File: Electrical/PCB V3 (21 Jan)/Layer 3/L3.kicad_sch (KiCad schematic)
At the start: 21 parts, among them J1 Conn_01x06, J2 Conn_02x04_Counter_Clockwise, J3 Conn_01x06, J4 Conn_01x06, J5 Conn_01x06, U2 113991054, U3 4754

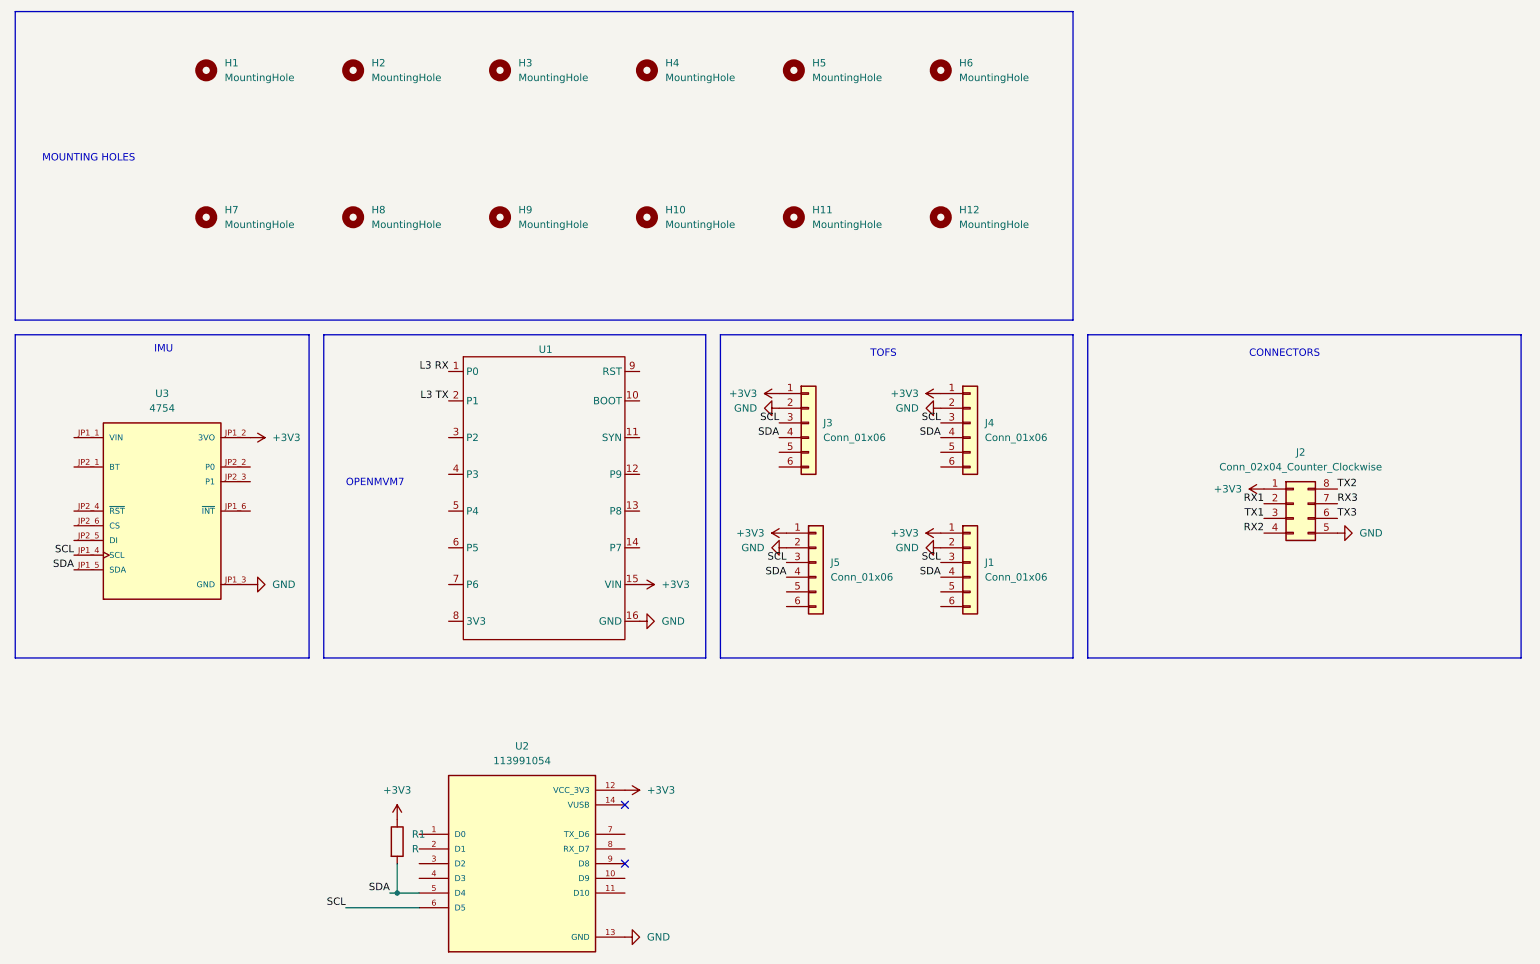
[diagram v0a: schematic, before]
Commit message: edited l3 schematics
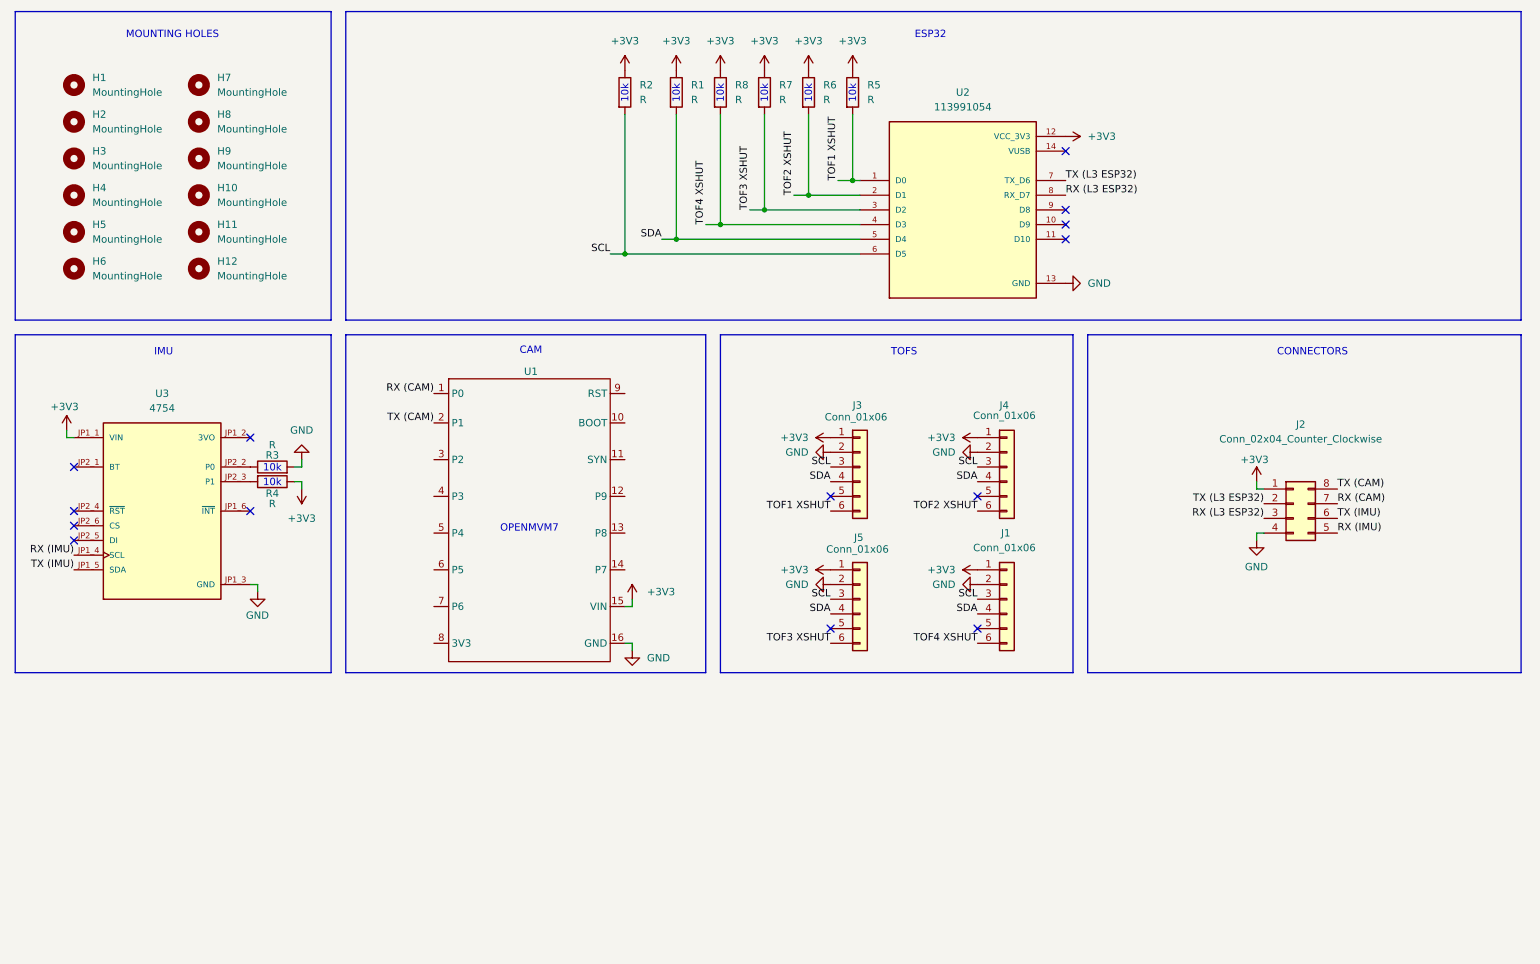
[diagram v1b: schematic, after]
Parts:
- added R2, R3, R4, R5, R6, R7, R8: R, symbol Device:R
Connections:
- net RX1 is gone; now on net TX (L3 ESP32): J2.2 (Pin_2)
- net RX2 is gone; now on net GND: J2.4 (Pin_4)
- net RX3 is gone; now on net RX (CAM): J2.7 (Pin_7)
- net TX1 is gone; now on net RX (L3 ESP32): J2.3 (Pin_3)
- net TX2 is gone; now on net TX (CAM): J2.8 (Pin_8)
- net +3V3: now also U3.JP1_1 (VIN), R2.1, R4.1, R5.1, R6.1, R7.1, R8.1; no longer U3.JP1_2 (3VO)
- net GND: now also R3.2; no longer J2.5 (Pin_5)
- net SCL: now also R2.2; no longer U3.JP1_4 (SCL)
- net SDA: no longer U3.JP1_5 (SDA)
- net TOF2 XSHUT: now reaches J4.6 (Pin_6)
- net TOF2 XSHUT: now also U2.2 (D1), R6.2
- net TOF4 XSHUT: now reaches J1.6 (Pin_6)
- net TOF4 XSHUT: now also U2.4 (D3), R8.2
- net TOF1 XSHUT: now reaches J3.6 (Pin_6)
- net TOF1 XSHUT: now also U2.1 (D0), R5.2
- net at U3.JP2_2 (P0): now also R3.1
- net at U3.JP2_3 (P1): now also R4.2
- net TOF3 XSHUT: now reaches U2.3 (D2)
- net TOF3 XSHUT: now also J5.6 (Pin_6), R7.2
- net TX (L3 ESP32): now reaches U2.7 (TX_D6)
- net RX (L3 ESP32): now reaches U2.8 (RX_D7)
- net L3 RX renamed RX (CAM)
- net L3 TX renamed TX (CAM)
- net TX3 renamed TX (IMU)
- net TX (IMU): now also U3.JP1_5 (SDA)
- new net RX (IMU): J2.5 (Pin_5), U3.JP1_4 (SCL)
- no-connect marks 2 -> 14
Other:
- note added: "10k"
- note added: "CAM"
- note added: "ESP32"
- moved on the sheet: H1, H10, H11, H12, H2, H3, H4, H5, H6, H7, H8, H9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

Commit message: roughly finished l3
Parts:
- R1, R2, R3, R4, R5, R6, R7, R8: footprint (none) -> Resistor_SMD:R_0603_1608Metric_Pad0.98x0.95mm_HandSolder
- U2: footprint Layer1_Symbol_Footprints:XiaoSeeedStudioEsp32 -> esp32_c3_xiao_seeed_studio:MODULE_113991054
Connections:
- net TOF2 XSHUT: now also J5.6 (Pin_6); no longer J4.6 (Pin_6)
- net TOF3 XSHUT: now also J4.6 (Pin_6); no longer J5.6 (Pin_6)
- no-connect marks 14 -> 26
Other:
- moved on the sheet: H1, H10, H11, H12, H2, H3, H4, H5, H6, H7, H8, H9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

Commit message: did some stuff with l3, settke another day
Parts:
- J2: value Conn_02x04_Counter_Clockwise -> Conn_02x04_Odd_Even; symbol Connector_Generic:Conn_02x04_Counter_Clockwise -> Connector_Generic:Conn_02x04_Odd_Even
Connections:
- net GND: now also J2.7 (Pin_7); no longer J2.4 (Pin_4)
- net RX (CAM): now also J2.4 (Pin_4); no longer J2.7 (Pin_7)
- net RX (IMU): now also J2.8 (Pin_8); no longer J2.5 (Pin_5)
- net RX (L3 ESP32): now also J2.5 (Pin_5); no longer J2.3 (Pin_3)
- net TX (CAM): now also J2.2 (Pin_2); no longer J2.8 (Pin_8)
- net TX (L3 ESP32): now also J2.3 (Pin_3); no longer J2.2 (Pin_2)
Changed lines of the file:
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@@
 	)
 	(symbol
-		(lib_id "Connector_Generic:Conn_02x04_Counter_Clockwise")
+		(lib_id "Connector_Generic:Conn_02x04_Odd_Even")
 		(at 240.03 123.19 0)
 		(unit 1)
@@
 			)
 		)
-		(property "Value" "Conn_02x04_Counter_Clockwise"
+		(property "Value" "Conn_02x04_Odd_Even"
 			(at 241.3 112.014 0)
 			(effects
@@
 			)
 		)
-		(property "Description" "Generic connector, double row, 02x04, counter clockwise pin numbering scheme (similar to DIP package numbering), script generated (kicad-library-utils/schlib/autogen/connector/)"
+		(property "Description" "Generic connector, double row, 02x04, odd/even pin numbering scheme (row 1 odd numbers, row 2 even numbers), script generated (kicad-library-utils/schlib/autogen/connector/)"
 			(at 240.03 123.19 0)
 			(effects

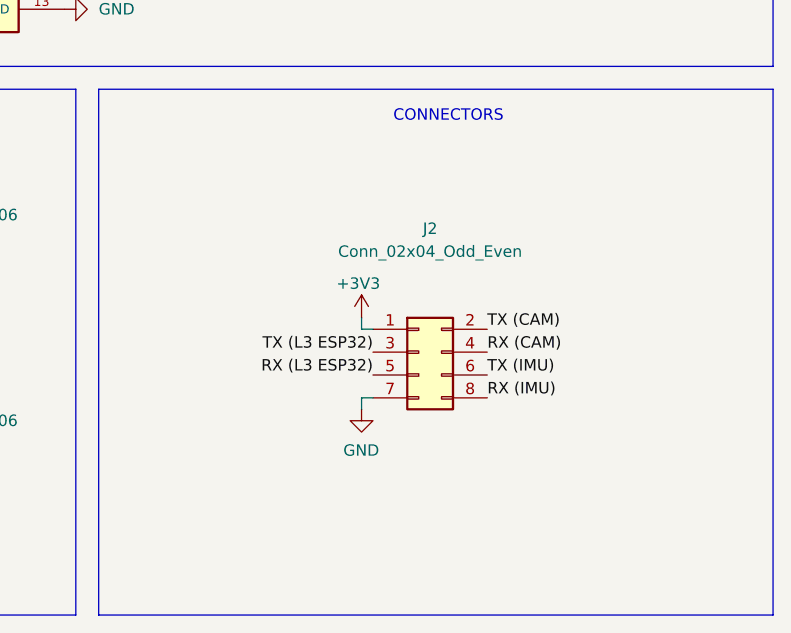
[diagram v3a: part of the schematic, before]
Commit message: switched l3 jst
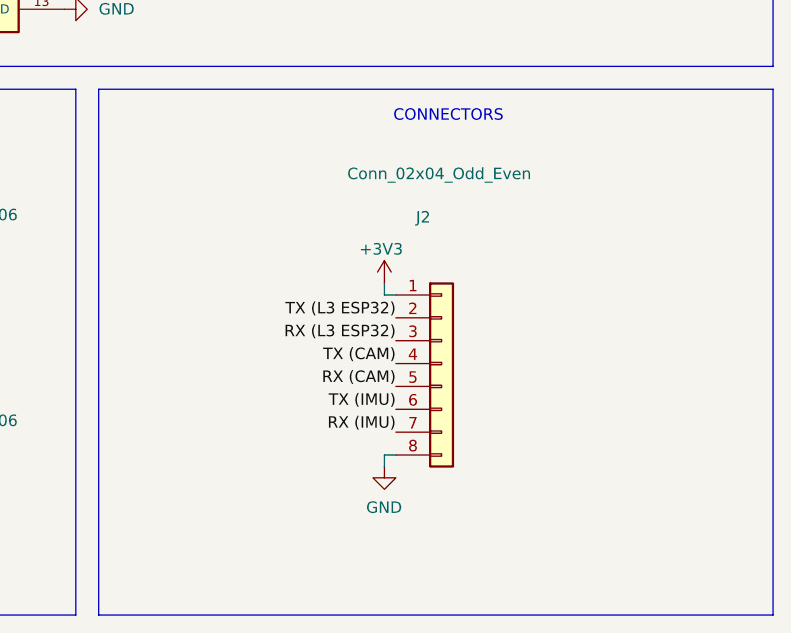
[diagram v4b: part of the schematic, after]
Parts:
- J2: footprint Connector_JST:JST_PHD_B8B-PHDSS_2x04_P2.00mm_Vertical -> Connector_JST:JST_EH_B8B-EH-A_1x08_P2.50mm_Vertical; symbol Connector_Generic:Conn_02x04_Odd_Even -> Connector_Generic:Conn_01x08
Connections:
- net GND: now also J2.8 (Pin_8); no longer J2.7 (Pin_7)
- net RX (CAM): now also J2.5 (Pin_5); no longer J2.4 (Pin_4)
- net RX (IMU): now also J2.7 (Pin_7); no longer J2.8 (Pin_8)
- net RX (L3 ESP32): now also J2.3 (Pin_3); no longer J2.5 (Pin_5)
- net TX (CAM): now also J2.4 (Pin_4); no longer J2.2 (Pin_2)
- net TX (L3 ESP32): now also J2.2 (Pin_2); no longer J2.3 (Pin_3)
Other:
- moved on the sheet: J2
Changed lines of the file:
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@@
 	(wire
 		(pts
-			(xy 148.59 55.88) (xy 148.59 72.39)
+			(xy 236.22 116.84) (xy 237.49 116.84)
 		)
 		(stroke
@@
 	(wire
 		(pts
-			(xy 124.46 80.01) (xy 165.1 80.01)
+			(xy 236.22 116.84) (xy 236.22 115.57)
 		)
 		(stroke
@@
 	(wire
 		(pts
-			(xy 125.73 147.32) (xy 124.46 147.32)
+			(xy 148.59 55.88) (xy 148.59 72.39)
 		)
 		(stroke
@@
 	(wire
 		(pts
-			(xy 124.46 55.88) (xy 124.46 80.01)
+			(xy 124.46 80.01) (xy 165.1 80.01)
 		)
 		(stroke
@@
 	(wire
 		(pts
-			(xy 67.31 116.84) (xy 68.58 116.84)
+			(xy 125.73 147.32) (xy 124.46 147.32)
 		)
 		(stroke
@@
 	(wire
 		(pts
-			(xy 125.73 140.97) (xy 125.73 139.7)
+			(xy 124.46 55.88) (xy 124.46 80.01)
 		)
 		(stroke
@@
 	(wire
 		(pts
-			(xy 233.68 120.65) (xy 234.95 120.65)
+			(xy 67.31 116.84) (xy 68.58 116.84)
+		)
+		(stroke
+			(width 0)
+			(type default)
+		)
+	)
+	(wire
+		(pts
+			(xy 125.73 140.97) (xy 125.73 139.7)
 		)
 		(stroke
@@
 	(wire
 		(pts
-			(xy 233.68 128.27) (xy 233.68 129.54)
+			(xy 236.22 134.62) (xy 236.22 135.89)
 		)
 		(stroke
@@
 	(wire
 		(pts
-			(xy 233.68 128.27) (xy 234.95 128.27)
-		)
-		(stroke
-			(width 0)
-			(type default)
-		)
-	)
-	(wire
-		(pts
 			(xy 161.29 67.31) (xy 163.83 67.31)
 		)
@@
 	(wire
 		(pts
-			(xy 156.21 69.85) (xy 165.1 69.85)
+			(xy 236.22 134.62) (xy 237.49 134.62)
 		)
 		(stroke
@@
 	(wire
 		(pts
-			(xy 67.31 119.38) (xy 68.58 119.38)
+			(xy 156.21 69.85) (xy 165.1 69.85)
 		)
 		(stroke
@@
 	(wire
 		(pts
-			(xy 233.68 120.65) (xy 233.68 119.38)
+			(xy 67.31 119.38) (xy 68.58 119.38)
 		)
 		(stroke
@@
 	)
 	(label "TX (CAM)"
-		(at 247.65 120.65 0)
+		(at 237.49 124.46 180)
 		(effects
 			(font
 				(size 1.27 1.27)
 			)
-			(justify left bottom)
+			(justify right bottom)
 		)
 	)
@@
 	)
 	(label "RX (CAM)"
-		(at 247.65 123.19 0)
+		(at 237.49 127 180)
 		(effects
 			(font
 				(size 1.27 1.27)
 			)
-			(justify left bottom)
+			(justify right bottom)
 		)
 	)
@@
 	)
 	(label "RX (L3 ESP32)"
-		(at 234.95 125.73 180)
+		(at 237.49 121.92 180)
 		(effects
 			(font
@@
 	)
 	(label "RX (IMU)"
-		(at 247.65 128.27 0)
+		(at 237.49 132.08 180)
 		(effects
 			(font
 				(size 1.27 1.27)
 			)
-			(justify left bottom)
+			(justify right bottom)
 		)
 	)
 	(label "TX (L3 ESP32)"
-		(at 234.95 123.19 180)
+		(at 237.49 119.38 180)
 		(effects
 			(font
@@
 	)
 	(label "TX (IMU)"
-		(at 247.65 125.73 0)
+		(at 237.49 129.54 180)
 		(effects
 			(font
 				(size 1.27 1.27)
 			)
-			(justify left bottom)
+			(justify right bottom)
 		)
 	)
@@
 	(symbol
 		(lib_id "power:+3V3")
-		(at 233.68 119.38 0)
+		(at 236.22 115.57 0)
 		(unit 1)
 		(exclude_from_sim no)
@@
 		(dnp no)
 		(property "Reference" "#PWR02"
-			(at 233.68 123.19 0)
+			(at 236.22 119.38 0)
 			(effects
 				(font
@@
 		)
 		(property "Value" "+3V3"
-			(at 230.886 115.57 0)
+			(at 233.426 111.76 0)
 			(effects
 				(font
@@
 		)
 		(property "Footprint" ""
-			(at 233.68 119.38 0)
+			(at 236.22 115.57 0)
 			(effects
 				(font
@@
 		)
 		(property "Datasheet" ""
-			(at 233.68 119.38 0)
+			(at 236.22 115.57 0)
 			(effects
 				(font
@@
 		)
 		(property "Description" "Power symbol creates a global label with name \"+3V3\""
-			(at 233.68 119.38 0)
+			(at 236.22 115.57 0)
 			(effects
 				(font
@@
 	)
 	(symbol
-		(lib_id "Connector_Generic:Conn_02x04_Odd_Even")
-		(at 240.03 123.19 0)
+		(lib_id "Connector_Generic:Conn_01x08")
+		(at 242.57 124.46 0)
 		(unit 1)
 		(exclude_from_sim no)
@@
 		(dnp no)
 		(property "Reference" "J2"
-			(at 241.3 109.474 0)
+			(at 240.538 108.204 0)
 			(effects
 				(font
@@
 		)
 		(property "Value" "Conn_02x04_Odd_Even"
-			(at 241.3 112.014 0)
+			(at 242.316 103.378 0)
 			(effects
 				(font
@@
 			)
 		)
-		(property "Footprint" "Connector_JST:JST_PHD_B8B-PHDSS_2x04_P2.00mm_Vertical"
-			(at 240.03 123.19 0)
+		(property "Footprint" "Connector_JST:JST_EH_B8B-EH-A_1x08_P2.50mm_Vertical"
+			(at 242.57 124.46 0)
 			(effects
 				(font
@@
 		)
 		(property "Datasheet" "~"
-			(at 240.03 123.19 0)
+			(at 242.57 124.46 0)
 			(effects
 				(font
@@
 			)
 		)
-		(property "Description" "Generic connector, double row, 02x04, odd/even pin numbering scheme (row 1 odd numbers, row 2 even numbers), script generated (kicad-library-utils/schlib/autogen/connector/)"
-			(at 240.03 123.19 0)
+		(property "Description" "Generic connector, single row, 01x08, script generated (kicad-library-utils/schlib/autogen/connector/)"
+			(at 242.57 124.46 0)
 			(effects
 				(font
@@
 	(symbol
 		(lib_id "power:GND")
-		(at 233.68 129.54 0)
+		(at 236.22 135.89 0)
 		(unit 1)
 		(exclude_from_sim no)
@@
 		(dnp no)
 		(property "Reference" "#PWR01"
-			(at 233.68 135.89 0)
+			(at 236.22 142.24 0)
 			(effects
 				(font
@@
 		)
 		(property "Value" "GND"
-			(at 231.648 134.112 0)
+			(at 234.188 140.462 0)
 			(effects
 				(font
@@
 		)
 		(property "Footprint" ""
-			(at 233.68 129.54 0)
+			(at 236.22 135.89 0)
 			(effects
 				(font
@@
 		)
 		(property "Datasheet" ""
-			(at 233.68 129.54 0)
+			(at 236.22 135.89 0)
 			(effects
 				(font
@@
 		)
 		(property "Description" "Power symbol creates a global label with name \"GND\" , ground"
-			(at 233.68 129.54 0)
+			(at 236.22 135.89 0)
 			(effects
 				(font

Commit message: deleted some l3 stuff to clear up folders, open and closed l3
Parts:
- J2: value Conn_02x04_Odd_Even -> Conn_02x08_Odd_Even
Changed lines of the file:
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@@
 			)
 		)
-		(property "Value" "Conn_02x04_Odd_Even"
+		(property "Value" "Conn_02x08_Odd_Even"
 			(at 242.316 103.378 0)
 			(effects

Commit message: fixed l2 caps positon, export new l2 step. fixed l3 jst from eh to xh, realised need to flip l2 jst
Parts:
- J2: footprint Connector_JST:JST_EH_B8B-EH-A_1x08_P2.50mm_Vertical -> Connector_JST:JST_XH_B10B-XH-A_1x10_P2.50mm_Vertical
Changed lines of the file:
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@@
 			)
 		)
-		(property "Footprint" "Connector_JST:JST_EH_B8B-EH-A_1x08_P2.50mm_Vertical"
+		(property "Footprint" "Connector_JST:JST_XH_B10B-XH-A_1x10_P2.50mm_Vertical"
 			(at 242.57 124.46 0)
 			(effects

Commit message: fixed l2, exported new l2 and l3 steps
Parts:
- J2: footprint Connector_JST:JST_XH_B10B-XH-A_1x10_P2.50mm_Vertical -> Connector_JST:JST_XH_B8B-XH-A_1x08_P2.50mm_Vertical
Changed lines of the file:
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@@
 			)
 		)
-		(property "Footprint" "Connector_JST:JST_XH_B10B-XH-A_1x10_P2.50mm_Vertical"
+		(property "Footprint" "Connector_JST:JST_XH_B8B-XH-A_1x08_P2.50mm_Vertical"
 			(at 242.57 124.46 0)
 			(effects
